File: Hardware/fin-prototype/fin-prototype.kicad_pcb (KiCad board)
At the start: 4 copper layers, 50 x 50 mm, 80 parts, among them J1 USB_C_Receptacle_USB2.0_16P, J10 Conn_01x01_Pin, J11 Conn_01x01_Pin, J12 Conn_01x01_Pin, J13 Conn_01x01_Pin, J14 Conn_01x01_Pin, J15 Conn_01x01_Pin, J16 Conn_01x01_Pin, J17 Conn_01x01_Pin, J18 Conn_01x01_Pin, J2 Conn_01x04_Pin, J3 Conn_01x04_Pin, J4 Conn_01x08_Pin, J5 Conn_01x04_Pin, J6 Conn_01x01_Pin, J7 Conn_01x01_Pin, J8 Conn_01x01_Pin, J9 Conn_01x01_Pin, SW1 SW_Push, SW2 SW_Push, U1 ADS131M03QPWRQ1, U2 STM32L412C8Tx, U3 W25N512GVEIG, U4 TMP235A4DBZR, U5 FT232RNQ-REEL

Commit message: place more components and silkscreen
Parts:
- added H1: MountingHole_Pad, MountingHole:MountingHole_2.2mm_M2_Pad, F.Cu at (141.5, 96.0)
- added H2: MountingHole_Pad, MountingHole:MountingHole_2.2mm_M2_Pad, F.Cu at (97.5, 96.0)
- added H3: MountingHole_Pad, MountingHole:MountingHole_2.2mm_M2_Pad, F.Cu at (97.5, 52.0)
- added H4: MountingHole_Pad, MountingHole:MountingHole_2.2mm_M2_Pad, F.Cu at (141.5, 52.0)
- added TP5: TestPoint, Connector_PinSocket_2.54mm:PinSocket_1x01_P2.54mm_Vertical, F.Cu at (141.5, 56.5)
- added TP6: TestPoint, Connector_PinSocket_2.54mm:PinSocket_1x01_P2.54mm_Vertical, F.Cu at (137.0, 96.0)
- added TP7: TestPoint, Connector_PinSocket_2.54mm:PinSocket_1x01_P2.54mm_Vertical, F.Cu at (97.5, 91.5)
- added TP8: TestPoint, Connector_PinSocket_2.54mm:PinSocket_1x01_P2.54mm_Vertical, F.Cu at (102.0, 52.0)
- J10, J11, J12, J13, J14, J15, J16, J17, J18, J6, J7, J8, J9: footprint Connector_PinHeader_2.54mm:PinHeader_1x01_P2.54mm_Vertical -> FinLib:SimpleThroughHole
- TP1, TP2, TP3, TP4: footprint TestPoint:TestPoint_Loop_D1.80mm_Drill1.0mm_Beaded -> Connector_PinHeader_2.54mm:PinHeader_1x01_P2.54mm_Vertical
- moved TP3 113.3 mm to (102.0, 96.0)
- moved TP2 112.5 mm to (97.5, 56.5)
- moved J16 77.1 mm to (102.0, 56.8), turned to 90 degrees
- moved J17 74.7 mm to (106.0, 56.8), turned to 90 degrees
- moved TP4 73.0 mm to (141.5, 91.5)
- moved TP1 73.0 mm to (137.0, 52.0)
- moved J18 72.8 mm to (110.0, 56.8), turned to 90 degrees
- moved J11 71.7 mm to (102.0, 60.5), turned to 90 degrees
- moved J15 69.9 mm to (114.0, 56.8), turned to 90 degrees
- moved J12 69.1 mm to (106.0, 60.5), turned to 90 degrees
- moved J13 67.1 mm to (110.0, 60.5), turned to 90 degrees
- moved J6 66.3 mm to (102.0, 64.2), turned to 90 degrees
- moved J14 65.5 mm to (114.0, 60.5), turned to 90 degrees
- moved J7 63.6 mm to (106.0, 64.2), turned to 90 degrees
- moved J8 61.4 mm to (110.0, 64.2), turned to 90 degrees
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- renumbered TP6 to TP10, TP7 to TP11, TP8 to TP12, TP9 to TP13, TP10 to TP14, TP11 to TP15, TP12 to TP16, TP13 to TP17, TP14 to TP18, TP15 to TP19, TP16 to TP20, TP17 to TP21, TP18 to TP22, TP19 to TP23, TP20 to TP24, TP21 to TP25, TP5 to TP9
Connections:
- net QSPI_CLK renamed QSPI_SCK
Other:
- outline, holes or cut-outs redrawn

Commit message: Revert "place more components and silkscreen"
This reverts commit 1bc8328d4b62153ca3fb5bb472924e08519ee507.
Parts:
- removed H1, H2, H3, H4: MountingHole_Pad, MountingHole:MountingHole_2.2mm_M2_Pad
- removed the TP5 at (141.5, 56.5)
- removed the TP6 at (137.0, 96.0)
- removed the TP7 at (97.5, 91.5)
- removed the TP8 at (102.0, 52.0)
- J10, J11, J12, J13, J14, J15, J16, J17, J18, J6, J7, J8, J9: footprint FinLib:SimpleThroughHole -> Connector_PinHeader_2.54mm:PinHeader_1x01_P2.54mm_Vertical
- TP1, TP2, TP3, TP4: footprint Connector_PinHeader_2.54mm:PinHeader_1x01_P2.54mm_Vertical -> TestPoint:TestPoint_Loop_D1.80mm_Drill1.0mm_Beaded
- moved TP3 113.3 mm to (210.0, 61.6)
- moved TP2 112.5 mm to (210.0, 56.9)
- moved J16 77.1 mm to (176.0, 78.3), turned to 0 degrees
- moved J17 74.7 mm to (176.0, 82.9), turned to 0 degrees
- moved TP4 73.0 mm to (210.0, 66.2)
- moved TP1 73.0 mm to (210.0, 52.3)
- moved J18 72.8 mm to (176.0, 87.5), turned to 0 degrees
- moved J11 71.7 mm to (171.4, 78.3), turned to 0 degrees
- moved J15 69.9 mm to (171.4, 96.7), turned to 0 degrees
- moved J12 69.1 mm to (171.4, 82.9), turned to 0 degrees
- moved J13 67.1 mm to (171.4, 87.5), turned to 0 degrees
- moved J6 66.3 mm to (166.8, 78.3), turned to 0 degrees
- moved J14 65.5 mm to (171.4, 92.1), turned to 0 degrees
- moved J7 63.6 mm to (166.8, 82.9), turned to 0 degrees
- moved J8 61.4 mm to (166.8, 87.5), turned to 0 degrees
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- renumbered TP14 to TP10, TP15 to TP11, TP16 to TP12, TP17 to TP13, TP18 to TP14, TP19 to TP15, TP20 to TP16, TP21 to TP17, TP22 to TP18, TP23 to TP19, TP24 to TP20, TP25 to TP21, TP9 to TP5, TP10 to TP6, TP11 to TP7, TP12 to TP8, TP13 to TP9
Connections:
- net QSPI_SCK renamed QSPI_CLK
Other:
- outline, holes or cut-outs redrawn

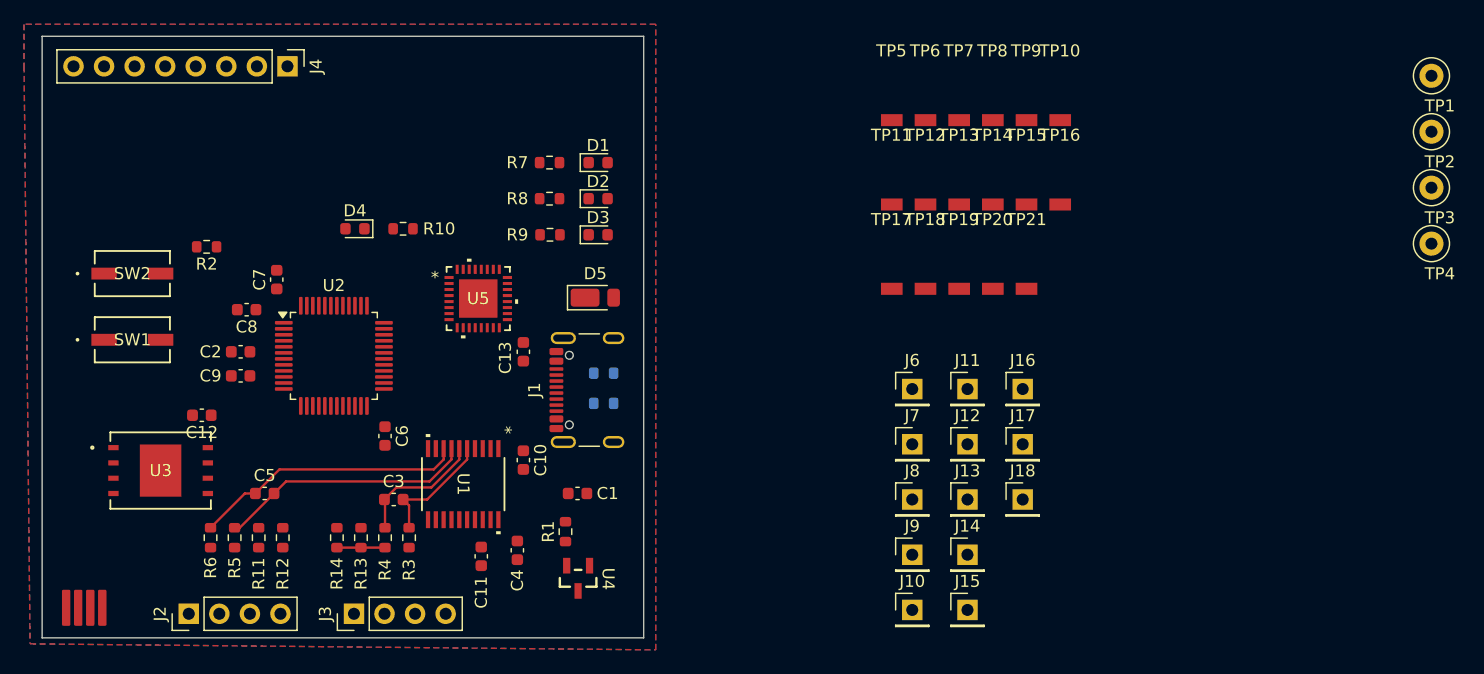
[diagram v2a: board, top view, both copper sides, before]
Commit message: all traces but test points
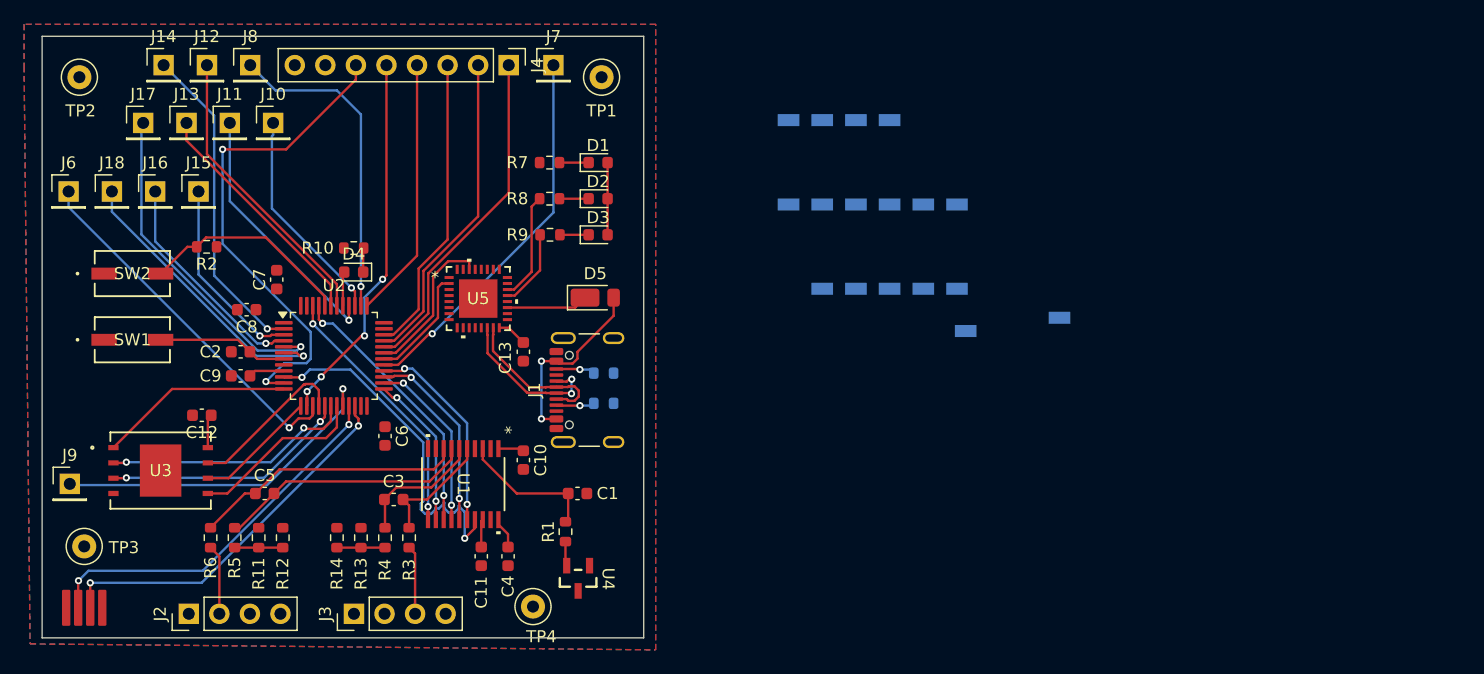
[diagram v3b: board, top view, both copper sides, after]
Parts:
- TP10, TP11, TP12, TP13, TP14, TP15, TP16, TP17, TP18, TP19, TP20, TP21, TP5, TP6, TP7, TP8, TP9: moved to B.Cu
- moved TP3 115.9 mm to (98.0, 91.4)
- moved TP2 112.5 mm to (97.6, 52.4)
- moved TP4 80.5 mm to (135.3, 96.4)
- moved J18 79.9 mm to (100.3, 61.9)
- moved J14 78.2 mm to (104.6, 51.4)
- moved J17 77.8 mm to (102.9, 56.2)
- moved J16 73.9 mm to (103.9, 61.9)
- moved J15 72.8 mm to (107.5, 61.9)
- moved J13 72.1 mm to (106.5, 56.2)
- moved J6 72.0 mm to (96.7, 61.9)
- moved J12 70.6 mm to (108.2, 51.4)
- moved J9 70.3 mm to (96.8, 86.2)
- moved TP1 69.0 mm to (141.0, 52.4)
- moved J10 66.8 mm to (113.7, 56.2)
- moved J8 65.8 mm to (111.8, 51.4)
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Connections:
- J4 pad 1: SPI1_MOSI -> SPI1_MISO
- J4 pad 2: SPI1_MISO -> SPI1_MOSI
- J4 pad 3: ~{SPI1_CS} -> SWDIO
- J4 pad 4: SPI1_SCK -> SWCLK
- J4 pad 5: SWDIO -> ~{SPI1_CS}
- J4 pad 6: SWCLK -> SPI1_SCK
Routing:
- net SPI1_SCK: track 0.00 -> 41.2 mm, vias 0 -> 2
- net SIGNAL: track 0.00 -> 31.7 mm, vias 0 -> 2
- net PA8: track 0.00 -> 31.6 mm, vias 0 -> 1
- net AVBAY_SYNC: track 0.00 -> 31.6 mm, vias 0 -> 2
- net ~{SPI1_CS}: track 0.00 -> 31.2 mm, vias 0 -> 4
- net PA5: track 0.00 -> 30.4 mm, vias 0 -> 1
- net TIM2_CH1: track 0.00 -> 29.7 mm, vias 0 -> 2
- net PB2: track 0.00 -> 28.5 mm, vias 0 -> 1
- net SPI1_MISO: track 0.00 -> 28.2 mm
- net PH0: track 0.00 -> 28.1 mm, vias 0 -> 1
- net PC13: track 0.00 -> 26.9 mm, vias 0 -> 1
- net PA15: track 0.00 -> 26.8 mm, vias 0 -> 1
- net SPI1_MOSI: track 0.00 -> 26.6 mm
- net SWDIO: track 0.00 -> 25.1 mm
- net PB6: track 0.00 -> 24.5 mm
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
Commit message: fixed some traces, placed test points in initial positions
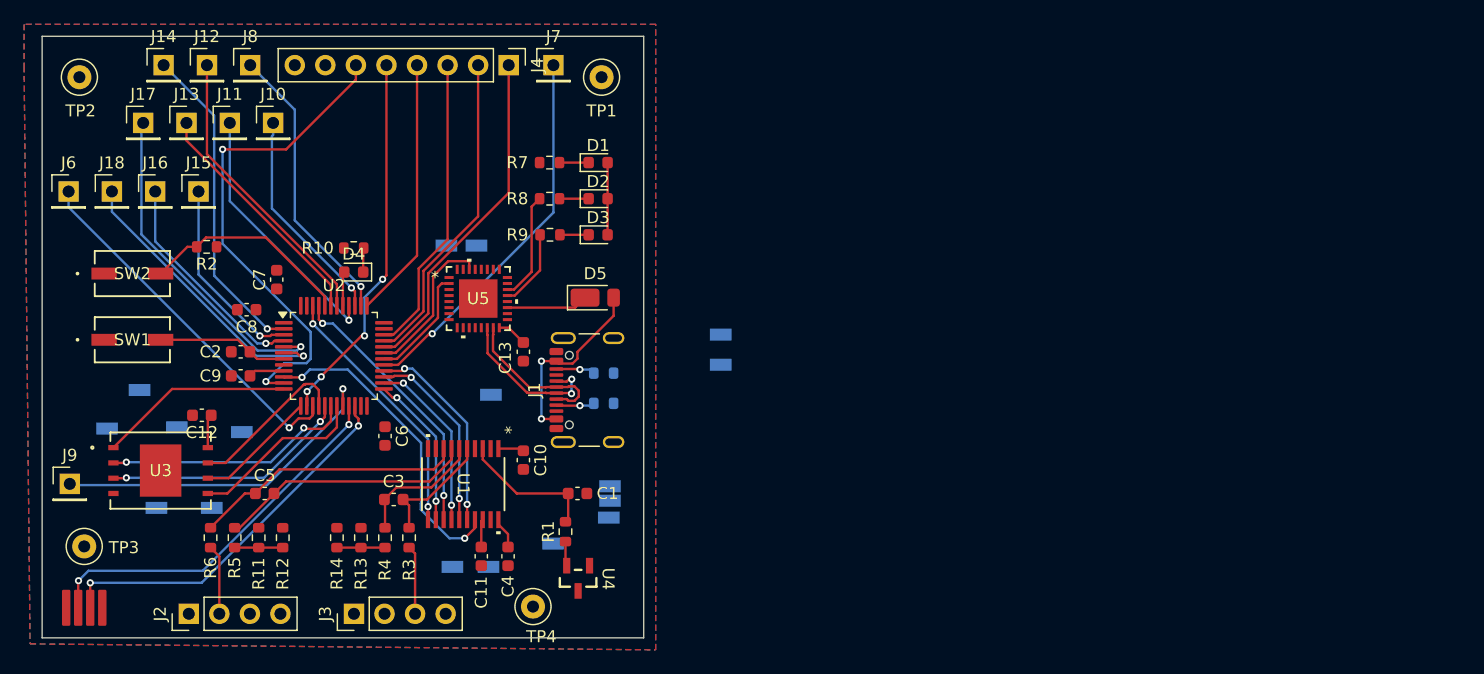
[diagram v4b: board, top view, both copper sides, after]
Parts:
- moved TP17 71.6 mm to (99.9, 76.3)
- moved TP13 66.0 mm to (104.0, 82.9)
- moved TP12 64.3 mm to (108.6, 82.9)
- moved TP14 61.5 mm to (102.6, 73.1)
- moved TP16 54.1 mm to (105.7, 76.2)
- moved TP15 51.8 mm to (111.1, 76.6)
- moved TP9 48.2 mm to (128.6, 87.8)
- moved TP8 48.1 mm to (131.6, 87.8)
- moved TP6 46.3 mm to (141.6, 94.3), turned to 0 degrees
- moved TP11 43.8 mm to (137.0, 85.9)
- moved TP7 40.2 mm to (131.8, 73.5)
- moved TP18 37.3 mm to (130.6, 61.1)
- moved TP19 37.0 mm to (128.1, 61.1)
- moved TP10 33.9 mm to (141.7, 81.1)
- moved TP5 32.8 mm to (141.7, 82.3)
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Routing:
- net TIM2_CH1: track 29.7 -> 26.3 mm
- net PA15: track 26.8 -> 23.8 mm
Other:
- board text added: "TODO: Add silkscreen labels TODO: Fix 3.3V layer TODO: See if traces can be routed in a less cursed way"
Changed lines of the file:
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@@
 	(footprint "FinLib:TestPoint"
 		(layer "B.Cu")
-		(at 170.57 64.73 180)
+		(at 99.93 76.34 180)
 		(property "Reference" "TP17"
 			(at 0 0.5 0)
@@
 	(footprint "FinLib:TestPoint"
 		(layer "B.Cu")
-		(at 170.57 57.72 180)
+		(at 137 85.9 180)
 		(property "Reference" "TP11"
 			(at 0 0.5 0)
@@
 	(footprint "FinLib:TestPoint"
 		(layer "B.Cu")
-		(at 167.77 64.73 180)
+		(at 130.63 61.14 180)
 		(property "Reference" "TP18"
 			(at 0 0.5 0)
@@
 	(footprint "FinLib:TestPoint"
 		(layer "B.Cu")
-		(at 162.17 57.72 180)
+		(at 102.63 73.14 180)
 		(property "Reference" "TP14"
 			(at 0 0.5 0)
@@
 	(footprint "FinLib:TestPoint"
 		(layer "B.Cu")
-		(at 162.17 50.71 180)
+		(at 131.63 87.84 180)
 		(property "Reference" "TP8"
 			(at 0 0.5 0)
@@
 	(footprint "FinLib:TestPoint"
 		(layer "B.Cu")
-		(at 164.97 64.73 180)
+		(at 128.13 61.14 180)
 		(property "Reference" "TP19"
 			(at 0 0.5 0)
@@
 	(footprint "FinLib:TestPoint"
 		(layer "B.Cu")
-		(at 156.57 57.72 180)
+		(at 105.73 76.24 180)
 		(property "Reference" "TP16"
 			(at 0 0.5 0)
@@
 	(footprint "FinLib:TestPoint"
 		(layer "B.Cu")
-		(at 167.77 57.72 180)
+		(at 108.63 82.94 180)
 		(property "Reference" "TP12"
 			(at 0 0.5 0)
@@
 	(footprint "FinLib:TestPoint"
 		(layer "B.Cu")
-		(at 162.17 64.73 180)
+		(at 150.93 68.535 180)
 		(property "Reference" "TP20"
 			(at 0 0.5 0)
@@
 	(footprint "FinLib:TestPoint"
 		(layer "B.Cu")
-		(at 164.97 57.72 180)
+		(at 104.03 82.94 180)
 		(property "Reference" "TP13"
 			(at 0 0.5 0)
@@
 	(footprint "FinLib:TestPoint"
 		(layer "B.Cu")
-		(at 159.37 57.72 180)
+		(at 111.13 76.64 180)
 		(property "Reference" "TP15"
 			(at 0 0.5 0)
@@
 	(footprint "FinLib:TestPoint"
 		(layer "B.Cu")
-		(at 179.09 67.14 180)
+		(at 141.57 94.26)
 		(property "Reference" "TP6"
-			(at 0 0.5 0)
+			(at 0 0.5 180)
 			(unlocked yes)
 			(layer "B.SilkS")
@@
 		)
 		(property "Value" "TestPoint"
-			(at 0 -1 0)
+			(at 0 -1 180)
 			(unlocked yes)
 			(layer "B.Fab")
@@
 		)
 		(property "Datasheet" ""
-			(at 0 0 0)
+			(at 0 0 180)
 			(unlocked yes)
 			(layer "B.Fab")
@@
 		)
 		(property "Description" "test point"
-			(at 0 0 0)
+			(at 0 0 180)
 			(unlocked yes)
 			(layer "B.Fab")
@@
 		(attr smd)
 		(fp_text user "${REFERENCE}"
-			(at 0 -2.5 0)
+			(at 0 -2.5 180)
 			(unlocked yes)
 			(layer "B.Fab")
@@
 		)
 		(pad "1" smd rect
-			(at 0.03 -5.26 180)
+			(at 0.03 -5.26)
 			(size 1.8 1)
 			(layers "B.Cu" "B.Mask" "B.Paste")
@@
 	(footprint "FinLib:TestPoint"
 		(layer "B.Cu")
-		(at 156.57 50.71 180)
+		(at 141.73 81.14 180)
 		(property "Reference" "TP10"
 			(at 0 0.5 0)
@@
 	(footprint "FinLib:TestPoint"
 		(layer "B.Cu")
-		(at 159.37 64.73 180)
+		(at 150.93 71.04 180)
 		(property "Reference" "TP21"
 			(at 0 0.5 0)
@@
 	(footprint "FinLib:TestPoint"
 		(layer "B.Cu")
-		(at 164.97 50.71 180)
+		(at 131.83 73.54 180)
 		(property "Reference" "TP7"
 			(at 0 0.5 0)
@@
 	(footprint "FinLib:TestPoint"
 		(layer "B.Cu")
-		(at 171.29 68.24 180)
+		(at 141.73 82.34 180)
 		(property "Reference" "TP5"
 			(at 0 0.5 0)
@@
 	(footprint "FinLib:TestPoint"
 		(layer "B.Cu")
-		(at 159.37 50.71 180)
+		(at 128.63 87.84 180)
 		(property "Reference" "TP9"
 			(at 0 0.5 0)
@@
 		(layer "Edge.Cuts")
 	)
+	(gr_text "TODO: Add silkscreen labels\nTODO: Fix 3.3V layer\nTODO: See if traces can be routed in a less cursed way"
+		(at 22.9 54.6 0)
+		(layer "Cmts.User")
+		(effects
+			(font
+				(size 1.5 1.5)
+				(thickness 0.3)
+				(bold yes)
+			)
+			(justify left bottom)
+		)
+	)
 	(segment
 		(start 133.947901 87)
@@
 	)
 	(segment
-		(start 113.9 53.5)
-		(end 111.8 51.4)
+		(start 121 69.8)
+		(end 115.5 64.3)
 		(width 0.2)
 		(layer "B.Cu")
@@
 	)
 	(segment
-		(start 119 53.5)
-		(end 113.9 53.5)
+		(start 115.5 55.1)
+		(end 114.4 54)
 		(width 0.2)
 		(layer "B.Cu")
@@
 	)
 	(segment
-		(start 121 55.5)
-		(end 119 53.5)
+		(start 115.5 64.3)
+		(end 115.5 55.1)
 		(width 0.2)
 		(layer "B.Cu")
@@
 	)
 	(segment
-		(start 121 69.8)
-		(end 121 55.5)
+		(start 114.4 54)
+		(end 111.8 51.4)
 		(width 0.2)
 		(layer "B.Cu")
@@
 	)
 	(segment
-		(start 127.837742 87.890868)
-		(end 127.485685 88.242925)
-		(width 0.2)
-		(layer "B.Cu")
-		(net 61)
-	)
-	(segment
-		(start 129.126 88.223943)
-		(end 128.773943 88.576)
-		(width 0.2)
-		(layer "B.Cu")
-		(net 61)
-	)
-	(segment
-		(start 126.176566 87.646293)
-		(end 126.176566 82.751566)
-		(width 0.2)
-		(layer "B.Cu")
-		(net 61)
-	)
-	(segment
-		(start 126.328623 88.696236)
-		(end 125.976566 88.344179)
-		(width 0.2)
-		(layer "B.Cu")
-		(net 61)
-	)
-	(segment
-		(start 127.178566 88.242925)
-		(end 127.178566 88.344179)
-		(width 0.2)
-		(layer "B.Cu")
-		(net 61)
-	)
-	(segment
-		(start 127.178566 88.344179)
-		(end 126.826509 88.696236)
-		(width 0.2)
-		(layer "B.Cu")
-		(net 61)
-	)
-	(segment
-		(start 128.276057 88.576)
-		(end 127.924 88.223943)
-		(width 0.2)
-		(layer "B.Cu")
-		(net 61)
-	)
-	(segment
-		(start 127.837742 87.770577)
-		(end 127.837742 87.890868)
-		(width 0.2)
-		(layer "B.Cu")
-		(net 61)
-	)
-	(segment
-		(start 125.976566 87.846293)
-		(end 126.176566 87.646293)
-		(width 0.2)
-		(layer "B.Cu")
-		(net 61)
-	)
-	(segment
-		(start 128.773943 88.576)
-		(end 128.276057 88.576)
-		(width 0.2)
-		(layer "B.Cu")
-		(net 61)
-	)
-	(segment
-		(start 127.485685 88.242925)
-		(end 127.178566 88.242925)
-		(width 0.2)
-		(layer "B.Cu")
-		(net 61)
-	)
-	(segment
-		(start 126.176566 82.751566)
-		(end 120.125 76.7)
-		(width 0.2)
-		(layer "B.Cu")
-		(net 61)
-	)
-	(segment
-		(start 129.224 88.148943)
-		(end 129.224 88.026)
-		(width 0.2)
-		(layer "B.Cu")
-		(net 61)
-	)
-	(segment
-		(start 127.924 88.223943)
-		(end 127.924 87.770577)
-		(width 0.2)
-		(layer "B.Cu")
-		(net 61)
-	)
-	(segment
-		(start 129.126 88.026)
-		(end 129.126 88.223943)
-		(width 0.2)
-		(layer "B.Cu")
-		(net 61)
-	)
-	(segment
-		(start 129.625 88.501)
-		(end 129.576057 88.501)
-		(width 0.2)
-		(layer "B.Cu")
-		(net 61)
-	)
-	(segment
-		(start 116.75 76.7)
+		(start 116.751 76.699)
 		(end 116.1 77.35)
 		(width 0.2)
@@
 	)
 	(segment
-		(start 129.576057 88.501)
-		(end 129.224 88.148943)
+		(start 125.976566 87.846293)
+		(end 126 87.822859)
 		(width 0.2)
 		(layer "B.Cu")
@@
 	)
 	(segment
-		(start 129.224 88.026)
-		(end 129.126 88.026)
+		(start 128.357387 90.725)
+		(end 125.976566 88.344179)
 		(width 0.2)
 		(layer "B.Cu")
@@
 	)
 	(segment
-		(start 126.826509 88.696236)
-		(end 126.328623 88.696236)
+		(start 129.625 90.725)
+		(end 128.357387 90.725)
 		(width 0.2)
 		(layer "B.Cu")
@@
 	)
 	(segment
-		(start 120.125 76.7)
-		(end 116.75 76.7)
+		(start 126 87.822859)
+		(end 126 82.8)
 		(width 0.2)
 		(layer "B.Cu")
@@
 	)
 	(segment
-		(start 127.924 87.770577)
-		(end 127.837742 87.770577)
+		(start 119.899 76.699)
+		(end 116.751 76.699)
 		(width 0.2)
 		(layer "B.Cu")
@@
 	)
 	(segment
-		(start 129.625 90.725)
-		(end 129.625 88.501)
+		(start 126 82.8)
+		(end 119.899 76.699)
 		(width 0.2)
 		(layer "B.Cu")
